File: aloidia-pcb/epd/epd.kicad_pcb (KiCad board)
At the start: 2 copper layers, 19.6 x 38.6 mm, 20 parts, among them J1 FH12-30S-0.5SH(55), J2 01x08 2.54mm Pin Headers

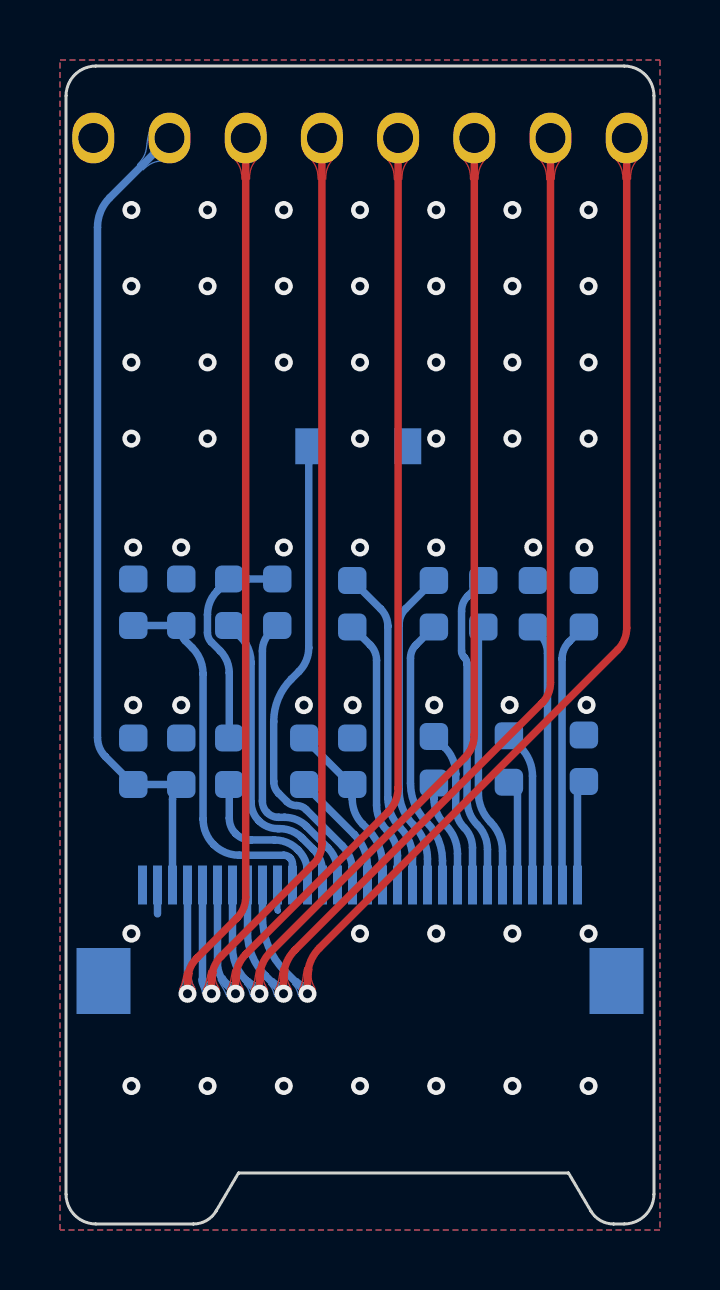
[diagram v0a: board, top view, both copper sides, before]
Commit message: Moved diode up
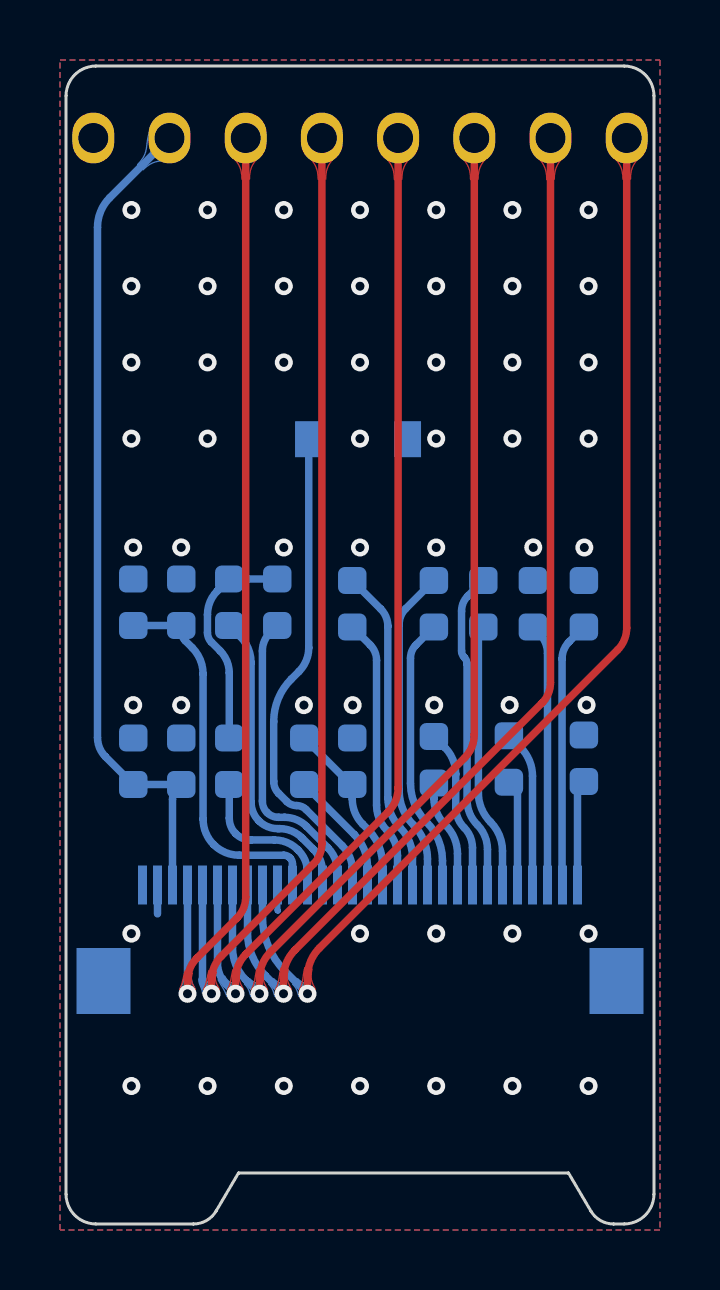
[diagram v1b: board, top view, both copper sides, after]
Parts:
- moved D1 0.23 mm to (157.7, 80.3)
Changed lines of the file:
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@@
   )
   (footprint "Diode_SMD:D_SOD-123" (layer "B.Cu")
-    (at 157.69232 80.574772 180)
+    (at 157.6842 80.3402 180)
     (descr "SOD-123")
     (tags "SOD-123")
